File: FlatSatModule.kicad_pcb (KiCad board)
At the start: 4 copper layers, 110.2 x 119.4 mm, 13 parts, among them J1 DB26_Male_HighDensity_Mountin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, J2 Micro_SD_Card_Det, J3 HEADER_13x2

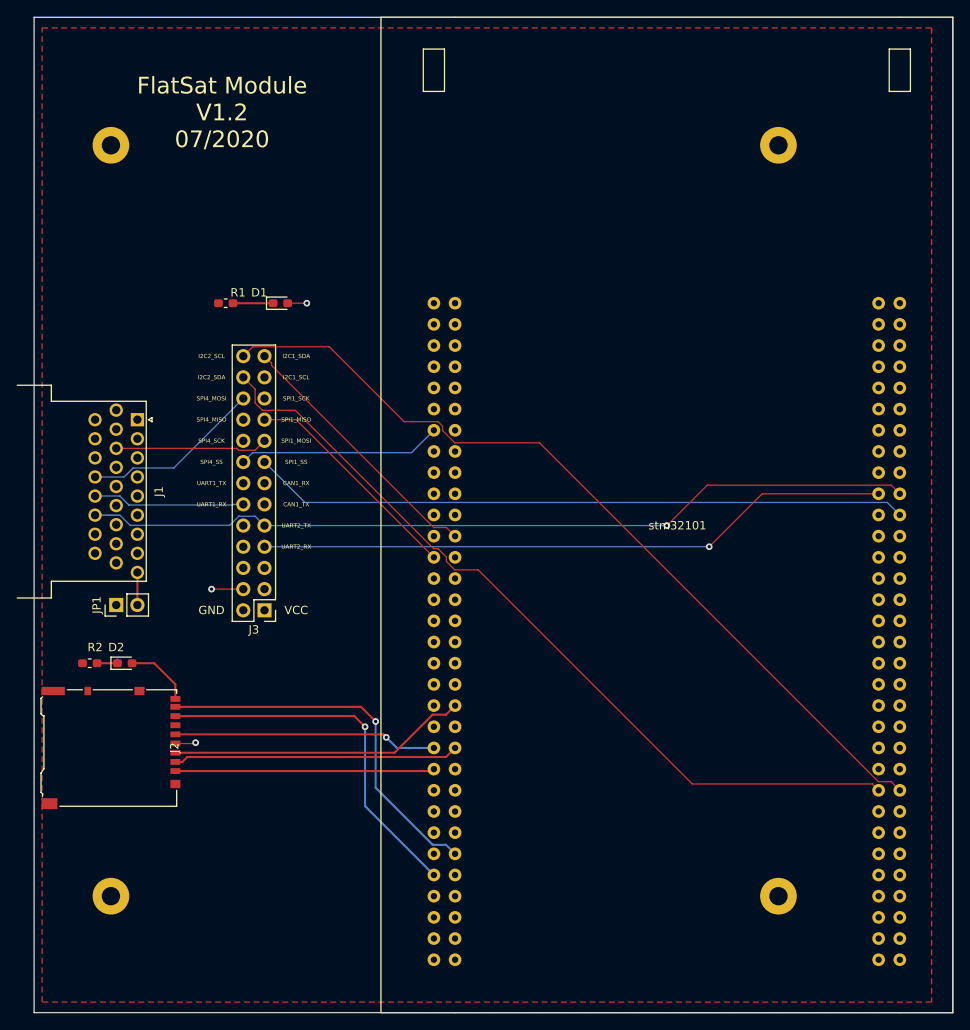
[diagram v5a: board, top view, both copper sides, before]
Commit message: Replaced DB 26 HD footprint, cleaned layout and few fixes...
Signed-off-by: Alexis Jeandet <alexis.jeandet@member.fsf.org>
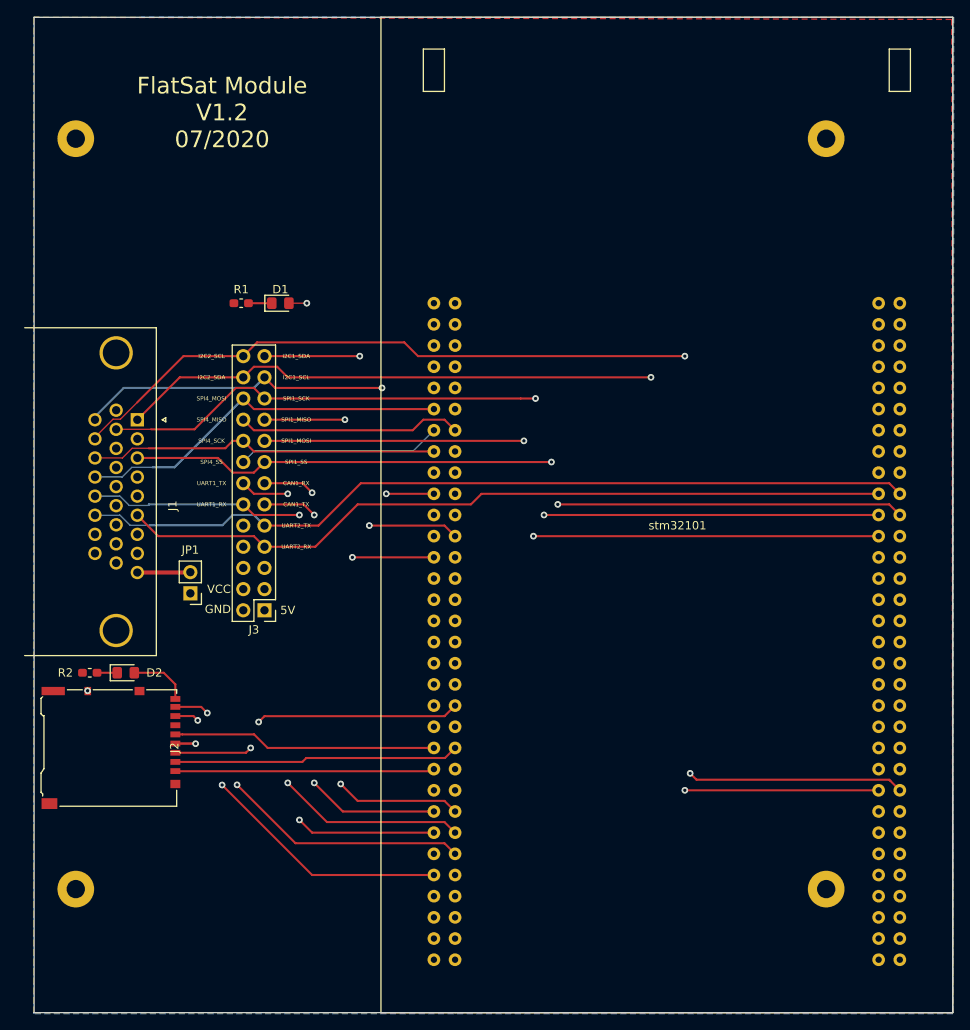
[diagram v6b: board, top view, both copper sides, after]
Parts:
- removed REF** (x4): MountingHole_2.2mm_M2_Pad, MountingHole:MountingHole_2.2mm_M2_Pad
- added H1: MountingHole_Pad, MountingHole:MountingHole_2.2mm_M2_Pad, F.Cu at (65.0, 132.5)
- added H2: MountingHole_Pad, MountingHole:MountingHole_2.2mm_M2_Pad, F.Cu at (65.0, 42.5)
- added H3: MountingHole_Pad, MountingHole:MountingHole_2.2mm_M2_Pad, F.Cu at (155.0, 132.5)
- added H4: MountingHole_Pad, MountingHole:MountingHole_2.2mm_M2_Pad, F.Cu at (155.0, 42.5)
- D1, D2: footprint LED_SMD:LED_0603_1608Metric_Pad1.05x0.95mm_HandSolder -> LED_SMD:LED_0805_2012Metric_Pad1.15x1.40mm_HandSolder
- J1: footprint Connector_Dsub:DSUB-26-HD_Male_Horizontal_P2.29x2.54mm_EdgePinOffset9.40mm -> DB-HD-26:DSUB-26-HD_Male_Horizontal_P2.29x1.98mm_EdgePinOffset8.35mm_Housed_MountingHolesOffset10.89mm
- moved JP1 9.00 mm to (78.7, 97.0), turned to 180 degrees
- moved R1 1.85 mm to (84.8, 62.2)
- moved D2 1.15 mm to (71.0, 106.6)
- moved R2 1.14 mm to (66.7, 106.6)
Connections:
- J1 pad 16: Net-(J1-Pad16) -> (no net)
- J1 pad 17: Net-(J1-Pad17) -> (no net)
- J1 pad 25: Net-(J1-Pad25) -> (no net)
- J1 pad 26: Net-(J1-Pad26) -> (no net)
- J1 pad 7: Net-(J1-Pad7) -> (no net)
- J1 pad 8: Net-(J1-Pad8) -> VCC
- J2 pad 10: (no net) -> VCC
- J2 pad 11: (no net) -> GND
- J3 pad 10: Net-(J3-Pad10) -> (no net)
- J3 pad 3: Net-(J3-Pad3) -> (no net)
- J3 pad 5: Net-(J3-Pad5) -> (no net)
- J3 pad 6: Net-(J3-Pad6) -> (no net)
- J3 pad 8: Net-(J3-Pad8) -> (no net)
- stm32101 pad 10: Net-(stm32101-Pad10) -> (no net)
- stm32101 pad 100: Net-(stm32101-Pad100) -> (no net)
- stm32101 pad 101: Net-(stm32101-Pad101) -> (no net)
- stm32101 pad 102: Net-(stm32101-Pad102) -> (no net)
- stm32101 pad 103: Net-(stm32101-Pad103) -> (no net)
- stm32101 pad 104: Net-(stm32101-Pad104) -> (no net)
- stm32101 pad 105: Net-(stm32101-Pad105) -> (no net)
- stm32101 pad 106: Net-(stm32101-Pad106) -> (no net)
- stm32101 pad 107: Net-(stm32101-Pad107) -> (no net)
- stm32101 pad 108: Net-(stm32101-Pad108) -> (no net)
- stm32101 pad 109: Net-(stm32101-Pad109) -> (no net)
- stm32101 pad 110: Net-(stm32101-Pad110) -> (no net)
- stm32101 pad 113: Net-(stm32101-Pad113) -> (no net)
- stm32101 pad 114: Net-(stm32101-Pad114) -> (no net)
- stm32101 pad 115: Net-(stm32101-Pad115) -> (no net)
- stm32101 pad 116: Net-(stm32101-Pad116) -> (no net)
- stm32101 pad 117: Net-(stm32101-Pad117) -> (no net)
- stm32101 pad 118: Net-(stm32101-Pad118) -> (no net)
- stm32101 pad 119: Net-(stm32101-Pad119) -> (no net)
- stm32101 pad 12: Net-(stm32101-Pad12) -> (no net)
- stm32101 pad 120: Net-(stm32101-Pad120) -> (no net)
- stm32101 pad 121: Net-(stm32101-Pad121) -> (no net)
- stm32101 pad 122: Net-(stm32101-Pad122) -> (no net)
- stm32101 pad 123: Net-(stm32101-Pad123) -> (no net)
- stm32101 pad 124: Net-(stm32101-Pad124) -> (no net)
- stm32101 pad 125: Net-(stm32101-Pad125) -> (no net)
- stm32101 pad 126: Net-(stm32101-Pad126) -> (no net)
- stm32101 pad 16: Net-(stm32101-Pad16) -> (no net)
- stm32101 pad 17: Net-(stm32101-Pad17) -> (no net)
- stm32101 pad 18: Net-(stm32101-Pad18) -> (no net)
- stm32101 pad 20: Net-(stm32101-Pad20) -> (no net)
- stm32101 pad 21: Net-(stm32101-Pad21) -> (no net)
- stm32101 pad 22: Net-(stm32101-Pad22) -> (no net)
- stm32101 pad 23: Net-(stm32101-Pad23) -> (no net)
- stm32101 pad 26: Net-(stm32101-Pad26) -> (no net)
- stm32101 pad 27: Net-(stm32101-Pad27) -> (no net)
- stm32101 pad 28: Net-(stm32101-Pad28) -> (no net)
- stm32101 pad 29: Net-(stm32101-Pad29) -> (no net)
- stm32101 pad 3: Net-(stm32101-Pad3) -> (no net)
- stm32101 pad 30: Net-(stm32101-Pad30) -> (no net)
- stm32101 pad 31: Net-(stm32101-Pad31) -> (no net)
- stm32101 pad 32: Net-(stm32101-Pad32) -> (no net)
- stm32101 pad 33: Net-(stm32101-Pad33) -> (no net)
- stm32101 pad 34: Net-(stm32101-Pad34) -> (no net)
- stm32101 pad 35: Net-(stm32101-Pad35) -> (no net)
- stm32101 pad 36: Net-(stm32101-Pad36) -> (no net)
- stm32101 pad 37: Net-(stm32101-Pad37) -> (no net)
- stm32101 pad 38: Net-(stm32101-Pad38) -> (no net)
- stm32101 pad 39: Net-(stm32101-Pad39) -> (no net)
- stm32101 pad 4: Net-(stm32101-Pad4) -> (no net)
- stm32101 pad 41: Net-(stm32101-Pad41) -> (no net)
- stm32101 pad 42: Net-(stm32101-Pad42) -> (no net)
- stm32101 pad 46: Net-(stm32101-Pad46) -> (no net)
- stm32101 pad 47: Net-(stm32101-Pad47) -> (no net)
- stm32101 pad 48: Net-(stm32101-Pad48) -> (no net)
- stm32101 pad 5: Net-(stm32101-Pad5) -> (no net)
- stm32101 pad 53: Net-(stm32101-Pad53) -> (no net)
- stm32101 pad 56: Net-(stm32101-Pad56) -> (no net)
- stm32101 pad 57: Net-(stm32101-Pad57) -> (no net)
- stm32101 pad 58: Net-(stm32101-Pad58) -> (no net)
- stm32101 pad 59: Net-(stm32101-Pad59) -> (no net)
- stm32101 pad 6: Net-(stm32101-Pad6) -> (no net)
- stm32101 pad 60: Net-(stm32101-Pad60) -> (no net)
- stm32101 pad 61: Net-(stm32101-Pad61) -> (no net)
- stm32101 pad 62: Net-(stm32101-Pad62) -> (no net)
- stm32101 pad 67: Net-(stm32101-Pad67) -> (no net)
- stm32101 pad 68: Net-(stm32101-Pad68) -> (no net)
- stm32101 pad 69: Net-(stm32101-Pad69) -> (no net)
- stm32101 pad 7: Net-(stm32101-Pad7) -> (no net)
- stm32101 pad 70: Net-(stm32101-Pad70) -> (no net)
- stm32101 pad 71: Net-(stm32101-Pad71) -> (no net)
- stm32101 pad 72: Net-(stm32101-Pad72) -> (no net)
- stm32101 pad 73: Net-(stm32101-Pad73) -> (no net)
- stm32101 pad 74: Net-(stm32101-Pad74) -> (no net)
- stm32101 pad 76: Net-(stm32101-Pad76) -> (no net)
- stm32101 pad 77: Net-(stm32101-Pad77) -> (no net)
- stm32101 pad 78: Net-(stm32101-Pad78) -> (no net)
- stm32101 pad 79: Net-(stm32101-Pad79) -> (no net)
- stm32101 pad 8: Net-(stm32101-Pad8) -> (no net)
- stm32101 pad 80: Net-(stm32101-Pad80) -> (no net)
- stm32101 pad 81: Net-(stm32101-Pad81) -> (no net)
- stm32101 pad 82: Net-(stm32101-Pad82) -> (no net)
- stm32101 pad 88: Net-(stm32101-Pad88) -> (no net)
- stm32101 pad 89: Net-(stm32101-Pad89) -> (no net)
- stm32101 pad 9: Net-(stm32101-Pad9) -> (no net)
- stm32101 pad 90: Net-(stm32101-Pad90) -> (no net)
- stm32101 pad 91: Net-(stm32101-Pad91) -> (no net)
- stm32101 pad 92: Net-(stm32101-Pad92) -> (no net)
- stm32101 pad 94: Net-(stm32101-Pad94) -> (no net)
- stm32101 pad 95: Net-(stm32101-Pad95) -> (no net)
- stm32101 pad 96: Net-(stm32101-Pad96) -> (no net)
- stm32101 pad 97: Net-(stm32101-Pad97) -> (no net)
- stm32101 pad 98: Net-(stm32101-Pad98) -> (no net)
- stm32101 pad 99: Net-(stm32101-Pad99) -> (no net)
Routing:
- net /I2C2_SDA: track 113.4 -> 154.0 mm, vias 0 -> 2
- net /I2C2_SCL: track 123.5 -> 152.7 mm, vias 0 -> 2
- net /UART1_RX: track 67.6 -> 78.8 mm, vias 0 -> 2
- net /I2C1_SDA: track 52.8 -> 63.5 mm, vias 0 -> 2
- net /UART1_TX: track 69.6 -> 79.5 mm, vias 0 -> 2
- net /CAN1_TX: track 61.0 -> 70.3 mm, vias 0 -> 2
- net /SPI1_MISO: track 45.0 -> 54.3 mm, vias 0 -> 2
- net /CAN1_RX: track 67.5 -> 76.1 mm, vias 0 -> 2
- net /SPI1_SCK: track 99.1 -> 107.4 mm, vias 0 -> 2
- net /I2C1_SCL: track 49.6 -> 55.9 mm, vias 0 -> 2
- net /SPI1_MOSI: track 96.7 -> 102.9 mm, vias 0 -> 2
- net VCC: track 8.59 -> 4.74 mm
- net /SPI1_SS: track 94.9 -> 97.9 mm, vias 0 -> 2
- net /SD_D0: track 44.5 -> 41.7 mm, vias 1 -> 2
- net /SPI4_MOSI: track 45.1 -> 47.7 mm
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- added copper zone on B.Cu, net GND
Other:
- rule trace_min: 0.00015 -> 0.15
- board text added: "5V"

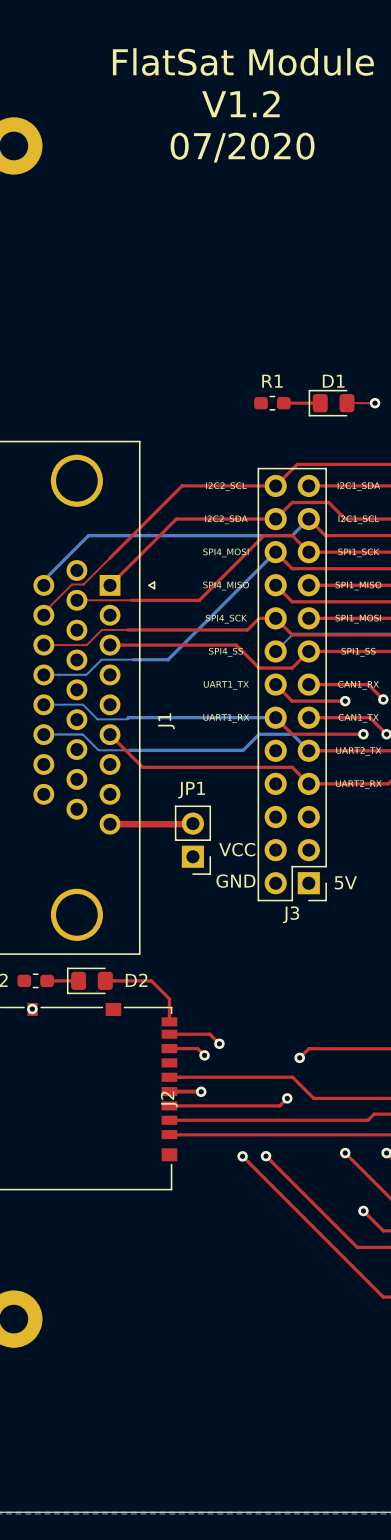
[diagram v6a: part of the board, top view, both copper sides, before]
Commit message: Add X logo, reset version to 1.0 and move microSD label
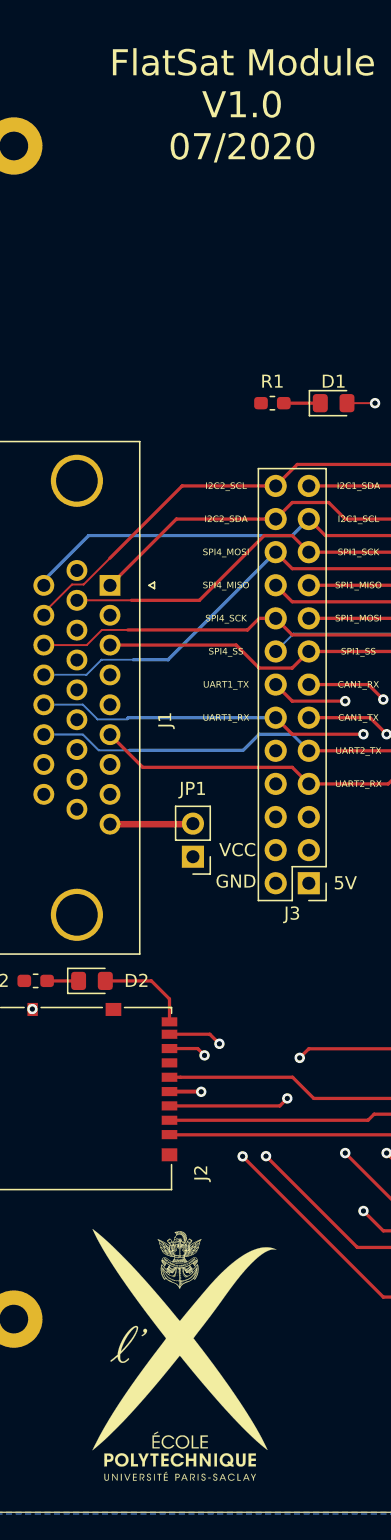
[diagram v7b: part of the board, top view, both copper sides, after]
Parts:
- added G1: LOGO, x-logo:X-LOGO, F.Cu at (78.1, 135.3)
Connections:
- J1 pad 16: (no net) -> Net-(J1-Pad16)
- J1 pad 17: (no net) -> Net-(J1-Pad17)
- J1 pad 25: (no net) -> Net-(J1-Pad25)
- J1 pad 26: (no net) -> Net-(J1-Pad26)
- J1 pad 7: (no net) -> Net-(J1-Pad7)
- J3 pad 10: (no net) -> Net-(J3-Pad10)
- J3 pad 3: (no net) -> Net-(J3-Pad3)
- J3 pad 5: (no net) -> Net-(J3-Pad5)
- J3 pad 6: (no net) -> Net-(J3-Pad6)
- J3 pad 8: (no net) -> Net-(J3-Pad8)
- stm32101 pad 10: (no net) -> Net-(stm32101-Pad10)
- stm32101 pad 100: (no net) -> Net-(stm32101-Pad100)
- stm32101 pad 101: (no net) -> Net-(stm32101-Pad101)
- stm32101 pad 102: (no net) -> Net-(stm32101-Pad102)
- stm32101 pad 103: (no net) -> Net-(stm32101-Pad103)
- stm32101 pad 104: (no net) -> Net-(stm32101-Pad104)
- stm32101 pad 105: (no net) -> Net-(stm32101-Pad105)
- stm32101 pad 106: (no net) -> Net-(stm32101-Pad106)
- stm32101 pad 107: (no net) -> Net-(stm32101-Pad107)
- stm32101 pad 108: (no net) -> Net-(stm32101-Pad108)
- stm32101 pad 109: (no net) -> Net-(stm32101-Pad109)
- stm32101 pad 110: (no net) -> Net-(stm32101-Pad110)
- stm32101 pad 113: (no net) -> Net-(stm32101-Pad113)
- stm32101 pad 114: (no net) -> Net-(stm32101-Pad114)
- stm32101 pad 115: (no net) -> Net-(stm32101-Pad115)
- stm32101 pad 116: (no net) -> Net-(stm32101-Pad116)
- stm32101 pad 117: (no net) -> Net-(stm32101-Pad117)
- stm32101 pad 118: (no net) -> Net-(stm32101-Pad118)
- stm32101 pad 119: (no net) -> Net-(stm32101-Pad119)
- stm32101 pad 12: (no net) -> Net-(stm32101-Pad12)
- stm32101 pad 120: (no net) -> Net-(stm32101-Pad120)
- stm32101 pad 121: (no net) -> Net-(stm32101-Pad121)
- stm32101 pad 122: (no net) -> Net-(stm32101-Pad122)
- stm32101 pad 123: (no net) -> Net-(stm32101-Pad123)
- stm32101 pad 124: (no net) -> Net-(stm32101-Pad124)
- stm32101 pad 125: (no net) -> Net-(stm32101-Pad125)
- stm32101 pad 126: (no net) -> Net-(stm32101-Pad126)
- stm32101 pad 16: (no net) -> Net-(stm32101-Pad16)
- stm32101 pad 17: (no net) -> Net-(stm32101-Pad17)
- stm32101 pad 18: (no net) -> Net-(stm32101-Pad18)
- stm32101 pad 20: (no net) -> Net-(stm32101-Pad20)
- stm32101 pad 21: (no net) -> Net-(stm32101-Pad21)
- stm32101 pad 22: (no net) -> Net-(stm32101-Pad22)
- stm32101 pad 23: (no net) -> Net-(stm32101-Pad23)
- stm32101 pad 26: (no net) -> Net-(stm32101-Pad26)
- stm32101 pad 27: (no net) -> Net-(stm32101-Pad27)
- stm32101 pad 28: (no net) -> Net-(stm32101-Pad28)
- stm32101 pad 29: (no net) -> Net-(stm32101-Pad29)
- stm32101 pad 3: (no net) -> Net-(stm32101-Pad3)
- stm32101 pad 30: (no net) -> Net-(stm32101-Pad30)
- stm32101 pad 31: (no net) -> Net-(stm32101-Pad31)
- stm32101 pad 32: (no net) -> Net-(stm32101-Pad32)
- stm32101 pad 33: (no net) -> Net-(stm32101-Pad33)
- stm32101 pad 34: (no net) -> Net-(stm32101-Pad34)
- stm32101 pad 35: (no net) -> Net-(stm32101-Pad35)
- stm32101 pad 36: (no net) -> Net-(stm32101-Pad36)
- stm32101 pad 37: (no net) -> Net-(stm32101-Pad37)
- stm32101 pad 38: (no net) -> Net-(stm32101-Pad38)
- stm32101 pad 39: (no net) -> Net-(stm32101-Pad39)
- stm32101 pad 4: (no net) -> Net-(stm32101-Pad4)
- stm32101 pad 41: (no net) -> Net-(stm32101-Pad41)
- stm32101 pad 42: (no net) -> Net-(stm32101-Pad42)
- stm32101 pad 46: (no net) -> Net-(stm32101-Pad46)
- stm32101 pad 47: (no net) -> Net-(stm32101-Pad47)
- stm32101 pad 48: (no net) -> Net-(stm32101-Pad48)
- stm32101 pad 5: (no net) -> Net-(stm32101-Pad5)
- stm32101 pad 53: (no net) -> Net-(stm32101-Pad53)
- stm32101 pad 56: (no net) -> Net-(stm32101-Pad56)
- stm32101 pad 57: (no net) -> Net-(stm32101-Pad57)
- stm32101 pad 58: (no net) -> Net-(stm32101-Pad58)
- stm32101 pad 59: (no net) -> Net-(stm32101-Pad59)
- stm32101 pad 6: (no net) -> Net-(stm32101-Pad6)
- stm32101 pad 60: (no net) -> Net-(stm32101-Pad60)
- stm32101 pad 61: (no net) -> Net-(stm32101-Pad61)
- stm32101 pad 62: (no net) -> Net-(stm32101-Pad62)
- stm32101 pad 67: (no net) -> Net-(stm32101-Pad67)
- stm32101 pad 68: (no net) -> Net-(stm32101-Pad68)
- stm32101 pad 69: (no net) -> Net-(stm32101-Pad69)
- stm32101 pad 7: (no net) -> Net-(stm32101-Pad7)
- stm32101 pad 70: (no net) -> Net-(stm32101-Pad70)
- stm32101 pad 71: (no net) -> Net-(stm32101-Pad71)
- stm32101 pad 72: (no net) -> Net-(stm32101-Pad72)
- stm32101 pad 73: (no net) -> Net-(stm32101-Pad73)
- stm32101 pad 74: (no net) -> Net-(stm32101-Pad74)
- stm32101 pad 76: (no net) -> Net-(stm32101-Pad76)
- stm32101 pad 77: (no net) -> Net-(stm32101-Pad77)
- stm32101 pad 78: (no net) -> Net-(stm32101-Pad78)
- stm32101 pad 79: (no net) -> Net-(stm32101-Pad79)
- stm32101 pad 8: (no net) -> Net-(stm32101-Pad8)
- stm32101 pad 80: (no net) -> Net-(stm32101-Pad80)
- stm32101 pad 81: (no net) -> Net-(stm32101-Pad81)
- stm32101 pad 82: (no net) -> Net-(stm32101-Pad82)
- stm32101 pad 88: (no net) -> Net-(stm32101-Pad88)
- stm32101 pad 89: (no net) -> Net-(stm32101-Pad89)
- stm32101 pad 9: (no net) -> Net-(stm32101-Pad9)
- stm32101 pad 90: (no net) -> Net-(stm32101-Pad90)
- stm32101 pad 91: (no net) -> Net-(stm32101-Pad91)
- stm32101 pad 92: (no net) -> Net-(stm32101-Pad92)
- stm32101 pad 94: (no net) -> Net-(stm32101-Pad94)
- stm32101 pad 95: (no net) -> Net-(stm32101-Pad95)
- stm32101 pad 96: (no net) -> Net-(stm32101-Pad96)
- stm32101 pad 97: (no net) -> Net-(stm32101-Pad97)
- stm32101 pad 98: (no net) -> Net-(stm32101-Pad98)
- stm32101 pad 99: (no net) -> Net-(stm32101-Pad99)
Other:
- board text added: "FlatSat Module V1.0 07/2020"
- board text removed: "FlatSat Module V1.2 07/2020"

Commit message: wire sd_det to stm32 and correct stm32 footprint
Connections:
- stm32101 pad 35: Net-(stm32101-Pad35) -> /SD_DET
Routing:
- net /SD_DET: track 7.25 -> 40.1 mm
- net /UART2_RX: track 93.1 -> 97.9 mm, vias 0 -> 2
- net /UART2_TX: track 100.7 -> 104.7 mm, vias 0 -> 2
- net /I2C2_SCL: track 152.7 -> 150.1 mm
- net /SPI1_SS: track 97.9 -> 95.8 mm
- net /SPI1_SCK: track 107.4 -> 105.5 mm
- net /SPI1_MOSI: track 102.9 -> 101.0 mm
